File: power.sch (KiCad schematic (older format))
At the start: 18 parts, among them J11 Screw_Terminal_01x02, J2 BATT_OUT, J3 BATT_IN, Q2 Q_PMOS_GDS, SW2 SW_SPST, U1 TPS3711, U5 P783F-Q24-S5-S

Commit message: Replaced tps3711 with different part which is in stock.
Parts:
- removed R3: 1M69, Resistor_SMD:R_1206_3216Metric_Pad1.30x1.75mm_HandSolder, symbol Device:R_US
- removed R4: 71k5, Resistor_SMD:R_1206_3216Metric_Pad1.30x1.75mm_HandSolder, symbol Device:R_US
- removed U1: TPS3711, Package_TO_SOT_SMD:SOT-23-6_Handsoldering, symbol New_Library:TPS3711
- added C2: 10n, Capacitor_SMD:C_1206_3216Metric_Pad1.33x1.80mm_HandSolder, symbol Device:C
- added U1: R3119, Package_TO_SOT_SMD:SOT-23-5_HandSoldering, symbol New_Library:R3119
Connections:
- wire segments 63 -> 59
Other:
- note added: "10.3v Threshold\n"
- note removed: "1% resistors (10v Cutoff)\n"
- moved on the sheet: TP1
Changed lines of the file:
@@
 	1    0    0    -1
 $EndComp
-$Comp
-L New_Library:TPS3711 U1
-U 1 1 618E2051
-P 2250 4950
-F 0 "U1" H 2250 5610 118 0000 C CNN
-F 1 "TPS3711" H 2250 5446 79  0000 C CNN
-F 2 "Package_TO_SOT_SMD:SOT-23-6_Handsoldering" H 2250 5450 118 0001 C CNN
-F 3 "" H 2250 5450 118 0001 C CNN
-	1    2250 4950
-	1    0    0    -1
-$EndComp
-$Comp
-L power:GND #PWR0102
-U 1 1 618E412F
-P 2950 5300
-F 0 "#PWR0102" H 2950 5050 50  0001 C CNN
-F 1 "GND" H 2955 5127 50  0000 C CNN
-F 2 "" H 2950 5300 50  0001 C CNN
-F 3 "" H 2950 5300 50  0001 C CNN
-	1    2950 5300
-	1    0    0    -1
-$EndComp
-Wire Wire Line
-	2700 4800 2950 4800
-Wire Wire Line
-	2950 4800 2950 4950
-Wire Wire Line
-	2700 4950 2950 4950
-Connection ~ 2950 4950
-Wire Wire Line
-	2950 4950 2950 5300
-Wire Wire Line
-	1800 4950 1650 4950
-Wire Wire Line
-	1650 4950 1650 5200
-$Comp
-L power:GND #PWR0103
-U 1 1 618EA162
-P 1650 5300
-F 0 "#PWR0103" H 1650 5050 50  0001 C CNN
-F 1 "GND" H 1655 5127 50  0000 C CNN
-F 2 "" H 1650 5300 50  0001 C CNN
-F 3 "" H 1650 5300 50  0001 C CNN
-	1    1650 5300
-	1    0    0    -1
-$EndComp
-Wire Wire Line
-	1800 4800 1400 4800
-$Comp
-L Device:R_US R3
-U 1 1 618F8E38
-P 1400 4650
-F 0 "R3" H 1468 4696 50  0000 L CNN
-F 1 "1M69" H 1468 4605 50  0000 L CNN
-F 2 "Resistor_SMD:R_1206_3216Metric_Pad1.30x1.75mm_HandSolder" V 1440 4640 50  0001 C CNN
-F 3 "~" H 1400 4650 50  0001 C CNN
-	1    1400 4650
-	1    0    0    -1
-$EndComp
-$Comp
-L Device:R_US R4
-U 1 1 618F9768
-P 1400 4950
-F 0 "R4" H 1468 4996 50  0000 L CNN
-F 1 "71k5" H 1468 4905 50  0000 L CNN
-F 2 "Resistor_SMD:R_1206_3216Metric_Pad1.30x1.75mm_HandSolder" V 1440 4940 50  0001 C CNN
-F 3 "~" H 1400 4950 50  0001 C CNN
-	1    1400 4950
-	1    0    0    -1
-$EndComp
-Connection ~ 1400 4800
-Wire Wire Line
-	1400 5100 1400 5200
-Wire Wire Line
-	1400 5200 1650 5200
-Connection ~ 1650 5200
-Wire Wire Line
-	1650 5200 1650 5300
-Text Notes 1250 5050 1    59   ~ 0
-1% resistors (10v Cutoff)\n
 Wire Wire Line
 	1800 4650 1750 4650
@@
 Wire Wire Line
 	1750 4500 1400 4500
-Connection ~ 1400 4500
 Wire Wire Line
 	1600 3900 1600 3850
@@
 Connection ~ 1400 3850
 Wire Wire Line
-	2700 4650 3300 4650
-Text Label 3300 4650 2    50   ~ 0
+	2600 4650 3200 4650
+Text Label 3200 4650 2    50   ~ 0
 POWEROFF_OD
 Wire Notes Line width 20
@@
 L Connector:TestPoint TP1
 U 1 1 61BA9CCB
-P 3300 4650
-F 0 "TP1" V 3254 4838 50  0000 L CNN
-F 1 "Poweroff" V 3345 4838 50  0000 L CNN
-F 2 "TestPoint:TestPoint_Pad_1.5x1.5mm" H 3500 4650 50  0001 C CNN
-F 3 "~" H 3500 4650 50  0001 C CNN
-	1    3300 4650
+P 3200 4650
+F 0 "TP1" V 3154 4838 50  0000 L CNN
+F 1 "Poweroff" V 3245 4838 50  0000 L CNN
+F 2 "TestPoint:TestPoint_Pad_1.5x1.5mm" H 3400 4650 50  0001 C CNN
+F 3 "~" H 3400 4650 50  0001 C CNN
+	1    3200 4650
 	0    1    1    0
 $EndComp
@@
 Text Label 2000 1050 2    50   ~ 0
 BATT_SWITCHED
+$Comp
+L New_Library:R3119 U1
+U 1 1 61B6C66F
+P 2200 4850
+F 0 "U1" H 2200 5518 118 0000 C CNN
+F 1 "R3119" H 2200 5325 118 0000 C CNN
+F 2 "Package_TO_SOT_SMD:SOT-23-5_HandSoldering" H 2050 5550 118 0001 C CNN
+F 3 "" H 2050 5550 118 0001 C CNN
+	1    2200 4850
+	1    0    0    -1
+$EndComp
+$Comp
+L power:GND #PWR0102
+U 1 1 61B76C8A
+P 1650 5450
+F 0 "#PWR0102" H 1650 5200 50  0001 C CNN
+F 1 "GND" H 1655 5277 50  0000 C CNN
+F 2 "" H 1650 5450 50  0001 C CNN
+F 3 "" H 1650 5450 50  0001 C CNN
+	1    1650 5450
+	1    0    0    -1
+$EndComp
+Wire Wire Line
+	1800 5100 1650 5100
+Wire Wire Line
+	1650 5100 1650 5250
+Wire Wire Line
+	1800 5250 1650 5250
+Connection ~ 1650 5250
+Wire Wire Line
+	1650 5250 1650 5450
+$Comp
+L Device:C C2
+U 1 1 61B79631
+P 2850 5350
+F 0 "C2" H 2965 5396 50  0000 L CNN
+F 1 "10n" H 2965 5305 50  0000 L CNN
+F 2 "Capacitor_SMD:C_1206_3216Metric_Pad1.33x1.80mm_HandSolder" H 2888 5200 50  0001 C CNN
+F 3 "~" H 2850 5350 50  0001 C CNN
+	1    2850 5350
+	1    0    0    -1
+$EndComp
+Wire Wire Line
+	2600 5100 2850 5100
+Wire Wire Line
+	2850 5100 2850 5200
+$Comp
+L power:GND #PWR0103
+U 1 1 61B7ADE2
+P 2850 5500
+F 0 "#PWR0103" H 2850 5250 50  0001 C CNN
+F 1 "GND" H 2855 5327 50  0000 C CNN
+F 2 "" H 2850 5500 50  0001 C CNN
+F 3 "" H 2850 5500 50  0001 C CNN
+	1    2850 5500
+	1    0    0    -1
+$EndComp
+Text Notes 1200 4850 0    50   ~ 0
+10.3v Threshold\n
 $EndSCHEMATC

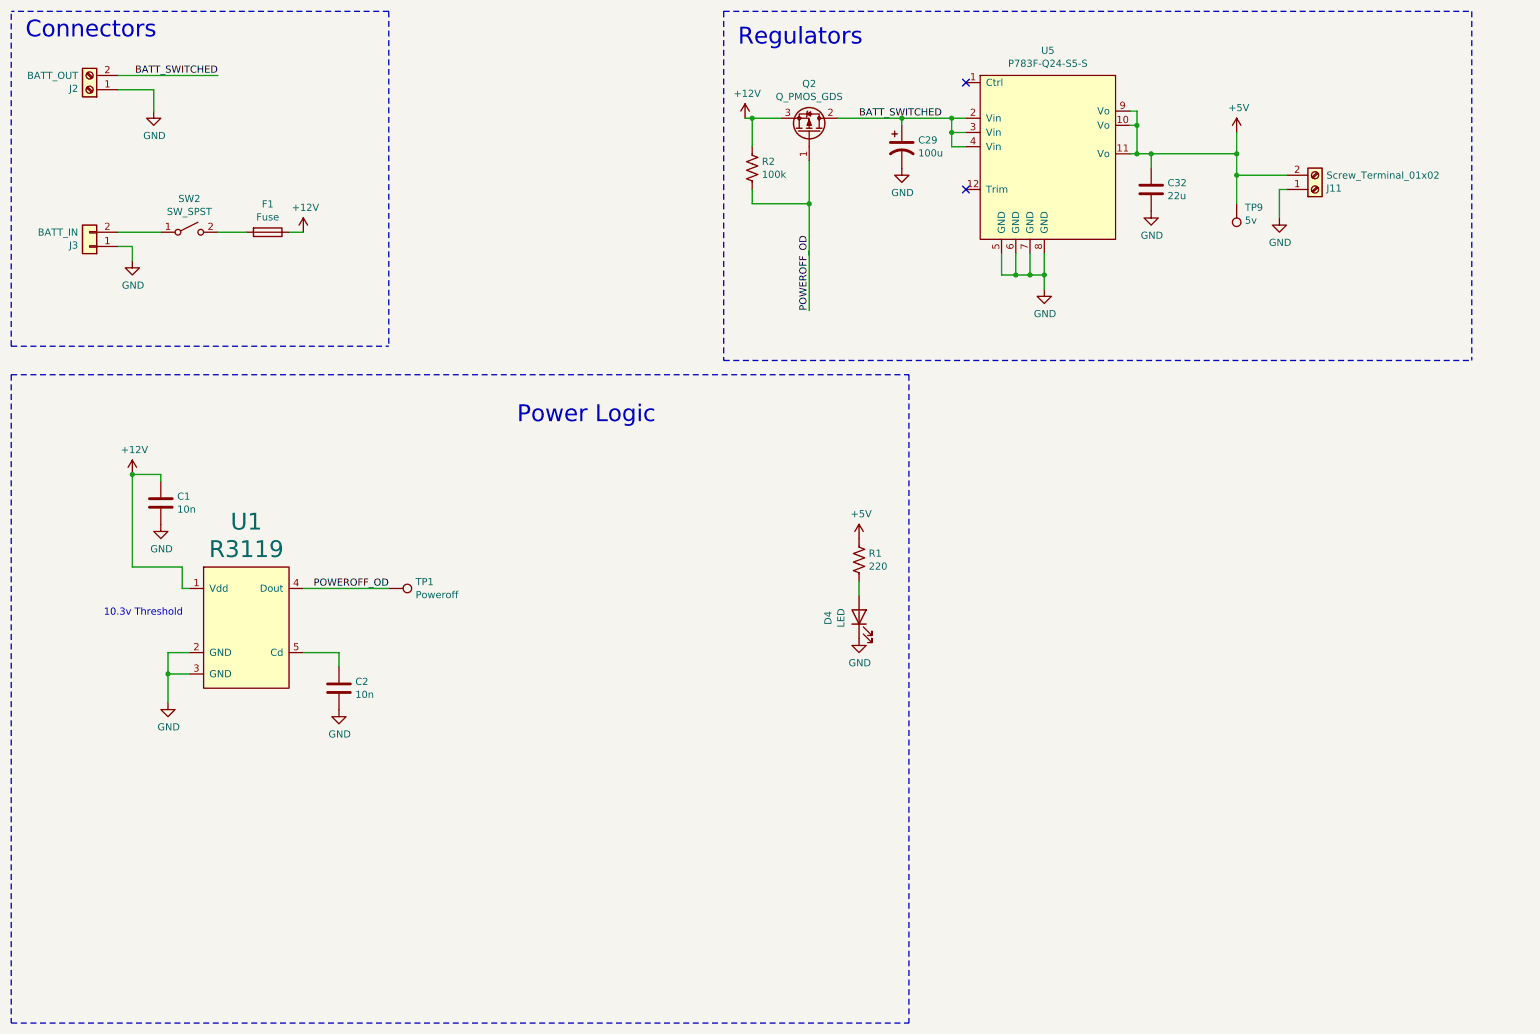
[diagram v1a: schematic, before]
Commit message: Swapped tps3711 for tl7702b because of availability. Added extra hysteresis to voltage supervisor.
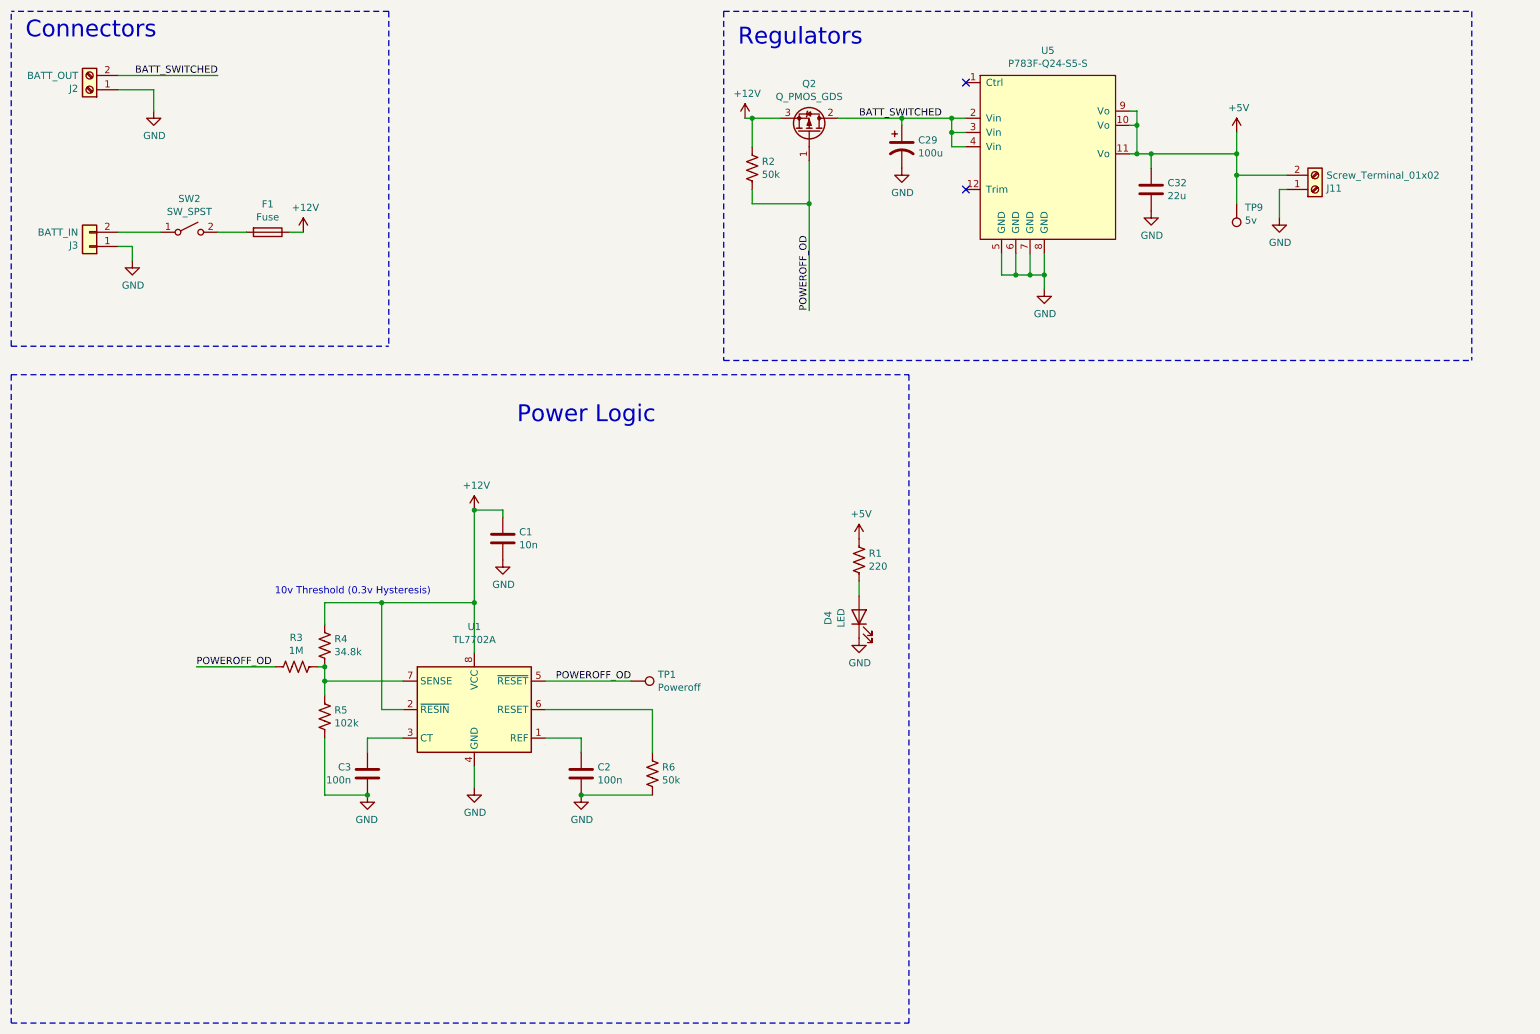
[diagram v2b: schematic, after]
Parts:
- removed U1: R3119, Package_TO_SOT_SMD:SOT-23-5_HandSoldering, symbol New_Library:R3119
- added C3: 100n, Capacitor_SMD:C_1206_3216Metric_Pad1.33x1.80mm_HandSolder, symbol Device:C
- added R3: 1M, Resistor_SMD:R_1206_3216Metric_Pad1.30x1.75mm_HandSolder, symbol Device:R_US
- added R4: 34.8k, Resistor_SMD:R_1206_3216Metric_Pad1.30x1.75mm_HandSolder, symbol Device:R_US
- added R5: 102k, Resistor_SMD:R_1206_3216Metric_Pad1.30x1.75mm_HandSolder, symbol Device:R_US
- added R6: 50k, Resistor_SMD:R_1206_3216Metric_Pad1.30x1.75mm_HandSolder, symbol Device:R_US
- added U1: TL7702A, Package_SO:SOIC-8_3.9x4.9mm_P1.27mm, symbol Power_Supervisor:TL7702A
- C2: value 10n -> 100n
- R2: value 100k -> 50k
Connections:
- net +12V: now also R4.1, U1.2 (~RESIN), U1.8 (VCC)
- net GND: now also C3.2, R5.2, R6.2, U1.4 (GND)
- net POWEROFF_OD: now also R3.1, U1.5 (~RESET)
- net at C2.1: now also U1.1 (REF)
- new net: C3.1, U1.3 (CT)
- new net: R6.1, U1.6 (RESET)
- new net: R3.2, R4.2, R5.1, U1.7 (SENSE)
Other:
- note added: "10v Threshold (0.3v Hysteresis)\n"
- note removed: "10.3v Threshold\n"
- moved on the sheet: C1, C2, TP1
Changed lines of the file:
@@
 	1    0    0    -1
 $EndComp
-Wire Wire Line
-	1800 4650 1750 4650
 $Comp
 L Device:C C1
 U 1 1 61908A2D
-P 1600 4050
-F 0 "C1" H 1715 4096 50  0000 L CNN
-F 1 "10n" H 1715 4005 50  0000 L CNN
-F 2 "Capacitor_SMD:C_1206_3216Metric_Pad1.33x1.80mm_HandSolder" H 1638 3900 50  0001 C CNN
-F 3 "~" H 1600 4050 50  0001 C CNN
-	1    1600 4050
+P 4000 4300
+F 0 "C1" H 4115 4346 50  0000 L CNN
+F 1 "10n" H 4115 4255 50  0000 L CNN
+F 2 "Capacitor_SMD:C_1206_3216Metric_Pad1.33x1.80mm_HandSolder" H 4038 4150 50  0001 C CNN
+F 3 "~" H 4000 4300 50  0001 C CNN
+	1    4000 4300
 	1    0    0    -1
 $EndComp
@@
 L power:GND #PWR0104
 U 1 1 61909975
-P 1600 4200
-F 0 "#PWR0104" H 1600 3950 50  0001 C CNN
-F 1 "GND" H 1605 4027 50  0000 C CNN
-F 2 "" H 1600 4200 50  0001 C CNN
-F 3 "" H 1600 4200 50  0001 C CNN
-	1    1600 4200
-	1    0    0    -1
-$EndComp
-Wire Wire Line
-	1400 3850 1400 4500
-Wire Wire Line
-	1750 4650 1750 4500
-Wire Wire Line
-	1750 4500 1400 4500
-Wire Wire Line
-	1600 3900 1600 3850
-Wire Wire Line
-	1600 3850 1400 3850
+P 4000 4450
+F 0 "#PWR0104" H 4000 4200 50  0001 C CNN
+F 1 "GND" H 4005 4277 50  0000 C CNN
+F 2 "" H 4000 4450 50  0001 C CNN
+F 3 "" H 4000 4450 50  0001 C CNN
+	1    4000 4450
+	1    0    0    -1
+$EndComp
+Wire Wire Line
+	4000 4150 4000 4100
+Wire Wire Line
+	4000 4100 3800 4100
 Wire Wire Line
 	8550 1600 9150 1600
@@
 L power:+12V #PWR0106
 U 1 1 61968CB4
-P 1400 3850
-F 0 "#PWR0106" H 1400 3700 50  0001 C CNN
-F 1 "+12V" H 1415 4023 50  0000 C CNN
-F 2 "" H 1400 3850 50  0001 C CNN
-F 3 "" H 1400 3850 50  0001 C CNN
-	1    1400 3850
-	1    0    0    -1
-$EndComp
-Connection ~ 1400 3850
-Wire Wire Line
-	2600 4650 3200 4650
-Text Label 3200 4650 2    50   ~ 0
+P 3800 4100
+F 0 "#PWR0106" H 3800 3950 50  0001 C CNN
+F 1 "+12V" H 3815 4273 50  0000 C CNN
+F 2 "" H 3800 4100 50  0001 C CNN
+F 3 "" H 3800 4100 50  0001 C CNN
+	1    3800 4100
+	1    0    0    -1
+$EndComp
+Connection ~ 3800 4100
+Wire Wire Line
+	4300 5300 4900 5300
+Text Label 4900 5300 2    50   ~ 0
 POWEROFF_OD
 Wire Notes Line width 20
@@
 L Connector:TestPoint TP1
 U 1 1 61BA9CCB
-P 3200 4650
-F 0 "TP1" V 3154 4838 50  0000 L CNN
-F 1 "Poweroff" V 3245 4838 50  0000 L CNN
-F 2 "TestPoint:TestPoint_Pad_1.5x1.5mm" H 3400 4650 50  0001 C CNN
-F 3 "~" H 3400 4650 50  0001 C CNN
-	1    3200 4650
+P 4900 5300
+F 0 "TP1" V 4854 5488 50  0000 L CNN
+F 1 "Poweroff" V 4945 5488 50  0000 L CNN
+F 2 "TestPoint:TestPoint_Pad_1.5x1.5mm" H 5100 5300 50  0001 C CNN
+F 3 "~" H 5100 5300 50  0001 C CNN
+	1    4900 5300
 	0    1    1    0
 $EndComp
@@
 P 5750 1700
 F 0 "R2" H 5818 1746 50  0000 L CNN
-F 1 "100k" H 5818 1655 50  0000 L CNN
+F 1 "50k" H 5818 1655 50  0000 L CNN
 F 2 "Resistor_SMD:R_1206_3216Metric_Pad1.30x1.75mm_HandSolder" V 5790 1690 50  0001 C CNN
 F 3 "~" H 5750 1700 50  0001 C CNN
@@
 BATT_SWITCHED
 $Comp
-L New_Library:R3119 U1
-U 1 1 61B6C66F
-P 2200 4850
-F 0 "U1" H 2200 5518 118 0000 C CNN
-F 1 "R3119" H 2200 5325 118 0000 C CNN
-F 2 "Package_TO_SOT_SMD:SOT-23-5_HandSoldering" H 2050 5550 118 0001 C CNN
-F 3 "" H 2050 5550 118 0001 C CNN
-	1    2200 4850
-	1    0    0    -1
-$EndComp
-$Comp
 L power:GND #PWR0102
 U 1 1 61B76C8A
-P 1650 5450
-F 0 "#PWR0102" H 1650 5200 50  0001 C CNN
-F 1 "GND" H 1655 5277 50  0000 C CNN
-F 2 "" H 1650 5450 50  0001 C CNN
-F 3 "" H 1650 5450 50  0001 C CNN
-	1    1650 5450
-	1    0    0    -1
-$EndComp
-Wire Wire Line
-	1800 5100 1650 5100
-Wire Wire Line
-	1650 5100 1650 5250
-Wire Wire Line
-	1800 5250 1650 5250
-Connection ~ 1650 5250
-Wire Wire Line
-	1650 5250 1650 5450
+P 3800 6050
+F 0 "#PWR0102" H 3800 5800 50  0001 C CNN
+F 1 "GND" H 3805 5877 50  0000 C CNN
+F 2 "" H 3800 6050 50  0001 C CNN
+F 3 "" H 3800 6050 50  0001 C CNN
+	1    3800 6050
+	1    0    0    -1
+$EndComp
 $Comp
 L Device:C C2
 U 1 1 61B79631
-P 2850 5350
-F 0 "C2" H 2965 5396 50  0000 L CNN
-F 1 "10n" H 2965 5305 50  0000 L CNN
-F 2 "Capacitor_SMD:C_1206_3216Metric_Pad1.33x1.80mm_HandSolder" H 2888 5200 50  0001 C CNN
-F 3 "~" H 2850 5350 50  0001 C CNN
-	1    2850 5350
-	1    0    0    -1
-$EndComp
-Wire Wire Line
-	2600 5100 2850 5100
-Wire Wire Line
-	2850 5100 2850 5200
+P 4550 5950
+F 0 "C2" H 4665 5996 50  0000 L CNN
+F 1 "100n" H 4665 5905 50  0000 L CNN
+F 2 "Capacitor_SMD:C_1206_3216Metric_Pad1.33x1.80mm_HandSolder" H 4588 5800 50  0001 C CNN
+F 3 "~" H 4550 5950 50  0001 C CNN
+	1    4550 5950
+	1    0    0    -1
+$EndComp
+Wire Wire Line
+	4300 5700 4550 5700
+Wire Wire Line
+	4550 5700 4550 5800
 $Comp
 L power:GND #PWR0103
 U 1 1 61B7ADE2
-P 2850 5500
-F 0 "#PWR0103" H 2850 5250 50  0001 C CNN
-F 1 "GND" H 2855 5327 50  0000 C CNN
-F 2 "" H 2850 5500 50  0001 C CNN
-F 3 "" H 2850 5500 50  0001 C CNN
-	1    2850 5500
-	1    0    0    -1
-$EndComp
-Text Notes 1200 4850 0    50   ~ 0
-10.3v Threshold\n
+P 4550 6100
+F 0 "#PWR0103" H 4550 5850 50  0001 C CNN
+F 1 "GND" H 4555 5927 50  0000 C CNN
+F 2 "" H 4550 6100 50  0001 C CNN
+F 3 "" H 4550 6100 50  0001 C CNN
+	1    4550 6100
+	1    0    0    -1
+$EndComp
+Text Notes 2400 4700 0    50   ~ 0
+10v Threshold (0.3v Hysteresis)\n
+$Comp
+L Power_Supervisor:TL7702A U1
+U 1 1 61BA0B82
+P 3800 5500
+F 0 "U1" H 3800 6081 50  0000 C CNN
+F 1 "TL7702A" H 3800 5990 50  0000 C CNN
+F 2 "Package_SO:SOIC-8_3.9x4.9mm_P1.27mm" H 3800 5500 50  0001 C CNN
+F 3 "http://www.ti.com.cn/cn/lit/ds/symlink/tl7705a.pdf" H 3800 5500 50  0001 C CNN
+	1    3800 5500
+	1    0    0    -1
+$EndComp
+Wire Wire Line
+	3800 5900 3800 6050
+$Comp
+L Device:C C3
+U 1 1 61BB72DC
+P 3050 5950
+F 0 "C3" H 3165 5996 50  0000 L CNN
+F 1 "100n" H 3165 5905 50  0000 L CNN
+F 2 "Capacitor_SMD:C_1206_3216Metric_Pad1.33x1.80mm_HandSolder" H 3088 5800 50  0001 C CNN
+F 3 "~" H 3050 5950 50  0001 C CNN
+	1    3050 5950
+	-1   0    0    -1
+$EndComp
+Wire Wire Line
+	3300 5700 3050 5700
+Wire Wire Line
+	3050 5700 3050 5800
+$Comp
+L power:GND #PWR0109
+U 1 1 61BB72E4
+P 3050 6100
+F 0 "#PWR0109" H 3050 5850 50  0001 C CNN
+F 1 "GND" H 3055 5927 50  0000 C CNN
+F 2 "" H 3050 6100 50  0001 C CNN
+F 3 "" H 3050 6100 50  0001 C CNN
+	1    3050 6100
+	-1   0    0    -1
+$EndComp
+$Comp
+L Device:R_US R6
+U 1 1 61BB877E
+P 5050 5950
+F 0 "R6" H 5118 5996 50  0000 L CNN
+F 1 "50k" H 5118 5905 50  0000 L CNN
+F 2 "Resistor_SMD:R_1206_3216Metric_Pad1.30x1.75mm_HandSolder" V 5090 5940 50  0001 C CNN
+F 3 "~" H 5050 5950 50  0001 C CNN
+	1    5050 5950
+	1    0    0    -1
+$EndComp
+Wire Wire Line
+	5050 5500 5050 5800
+Wire Wire Line
+	4550 6100 5050 6100
+Connection ~ 4550 6100
+Wire Wire Line
+	4300 5500 5050 5500
+Wire Wire Line
+	3800 4100 3800 4750
+Wire Wire Line
+	3300 5500 3150 5500
+Wire Wire Line
+	3150 5500 3150 4750
+Wire Wire Line
+	3150 4750 3800 4750
+Connection ~ 3800 4750
+Wire Wire Line
+	3800 4750 3800 5100
+$Comp
+L Device:R_US R4
+U 1 1 61BCCEB5
+P 2750 5050
+F 0 "R4" H 2818 5096 50  0000 L CNN
+F 1 "34.8k" H 2818 5005 50  0000 L CNN
+F 2 "Resistor_SMD:R_1206_3216Metric_Pad1.30x1.75mm_HandSolder" V 2790 5040 50  0001 C CNN
+F 3 "~" H 2750 5050 50  0001 C CNN
+	1    2750 5050
+	1    0    0    -1
+$EndComp
+$Comp
+L Device:R_US R5
+U 1 1 61BCD5FF
+P 2750 5550
+F 0 "R5" H 2818 5596 50  0000 L CNN
+F 1 "102k" H 2818 5505 50  0000 L CNN
+F 2 "Resistor_SMD:R_1206_3216Metric_Pad1.30x1.75mm_HandSolder" V 2790 5540 50  0001 C CNN
+F 3 "~" H 2750 5550 50  0001 C CNN
+	1    2750 5550
+	1    0    0    -1
+$EndComp
+Wire Wire Line
+	2750 4900 2750 4750
+Wire Wire Line
+	2750 4750 3150 4750
+Connection ~ 3150 4750
+Wire Wire Line
+	2750 5200 2750 5300
+Wire Wire Line
+	2750 5300 3300 5300
+Connection ~ 2750 5300
+Wire Wire Line
+	2750 5300 2750 5400
+Wire Wire Line
+	2750 5700 2750 6100
+Wire Wire Line
+	2750 6100 3050 6100
+Connection ~ 3050 6100
+Text Label 1850 5200 0    50   ~ 0
+POWEROFF_OD
+$Comp
+L Device:R_US R3
+U 1 1 61BDFB83
+P 2550 5200
+F 0 "R3" V 2755 5200 50  0000 C CNN
+F 1 "1M" V 2664 5200 50  0000 C CNN
+F 2 "Resistor_SMD:R_1206_3216Metric_Pad1.30x1.75mm_HandSolder" V 2590 5190 50  0001 C CNN
+F 3 "~" H 2550 5200 50  0001 C CNN
+	1    2550 5200
+	0    -1   -1   0
+$EndComp
+Wire Wire Line
+	2700 5200 2750 5200
+Connection ~ 2750 5200
+Wire Wire Line
+	1850 5200 2400 5200
 $EndSCHEMATC

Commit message: Many changes from first design review.
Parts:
- removed J11: Screw_Terminal_01x02, TerminalBlock:TerminalBlock_bornier-2_P5.08mm, symbol Connector:Screw_Terminal_01x02
- removed J2: BATT_OUT, TerminalBlock:TerminalBlock_bornier-2_P5.08mm, symbol Connector:Screw_Terminal_01x02
- added J4: V_ORBITTY, Connector_JST:JST_XH_S2B-XH-A_1x02_P2.50mm_Horizontal, symbol Connector_Generic:Conn_01x02
- added J5: V_HUB, Connector_JST:JST_XH_S2B-XH-A_1x02_P2.50mm_Horizontal, symbol Connector_Generic:Conn_01x02
- added R10, R9: 500k, Resistor_SMD:R_1206_3216Metric_Pad1.30x1.75mm_HandSolder, symbol Device:R_US
- added RV1: 1M, Potentiometer_SMD:Potentiometer_Bourns_3269W_Vertical, symbol Device:R_POT_TRIM_US
- added TP3: 12v, TestPoint:TestPoint_Plated_Hole_D2.0mm, symbol Connector:TestPoint
- D4: value LED -> PWR_LED
- J3: value BATT_IN -> EXT_PWR
- J6: renamed from SW2; value SW_SPST -> PWR_SWITCH; symbol Switch:SW_SPST -> Connector_Generic:Conn_01x02
- R1: value 220 -> 90
- TP1, TP9: footprint TestPoint:TestPoint_Pad_1.5x1.5mm -> TestPoint:TestPoint_Plated_Hole_D2.0mm
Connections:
- net BATT_SWITCHED is gone; now on net +12V: C29.1, Q2.2 (D), U5.2 (Vin), U5.3 (Vin), U5.4 (Vin)
- net +12V: now also J4.1 (Pin_1), TP3.1; no longer C1.1, F1.1, Q2.3 (S), R2.1, R4.1, U1.2 (~RESIN), U1.8 (VCC)
- net +5V: now also J5.1 (Pin_1), R9.1, RV1.3
- net GND: now also J4.2 (Pin_2), J5.2 (Pin_2), R10.2, RV1.1
- net at U5.12 (Trim): now also R10.1, R9.2, RV1.2
- new net Vext: C1.1, F1.1, Q2.3 (S), R2.1, R4.1, U1.2 (~RESIN), U1.8 (VCC)
- no-connect marks 2 -> 1
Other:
- note added: "20mA LED current, with 3.2V voltage drop"
- note added: "3A Rating"
- note added: "72mW max dissipation at 3A load"
- note added: "DNP RV1, R9, R10 unless needed"
- note added: "Max Current Draw 0.5A"
- note added: "Max Current Draw 2A"
- note added: "Regulator"
- note removed: "Regulators"
- moved on the sheet: C1, C2, C29, C3, C32, D4, F1, J3, Q2, R1, R2, R3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
